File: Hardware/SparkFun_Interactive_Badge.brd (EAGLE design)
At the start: 17.8 x 63.5 mm, 34 parts, among them Q1 DMG2307L, U1 MIC5205-3.3V, U2 ATMEGA328P, U3 CY7C65213

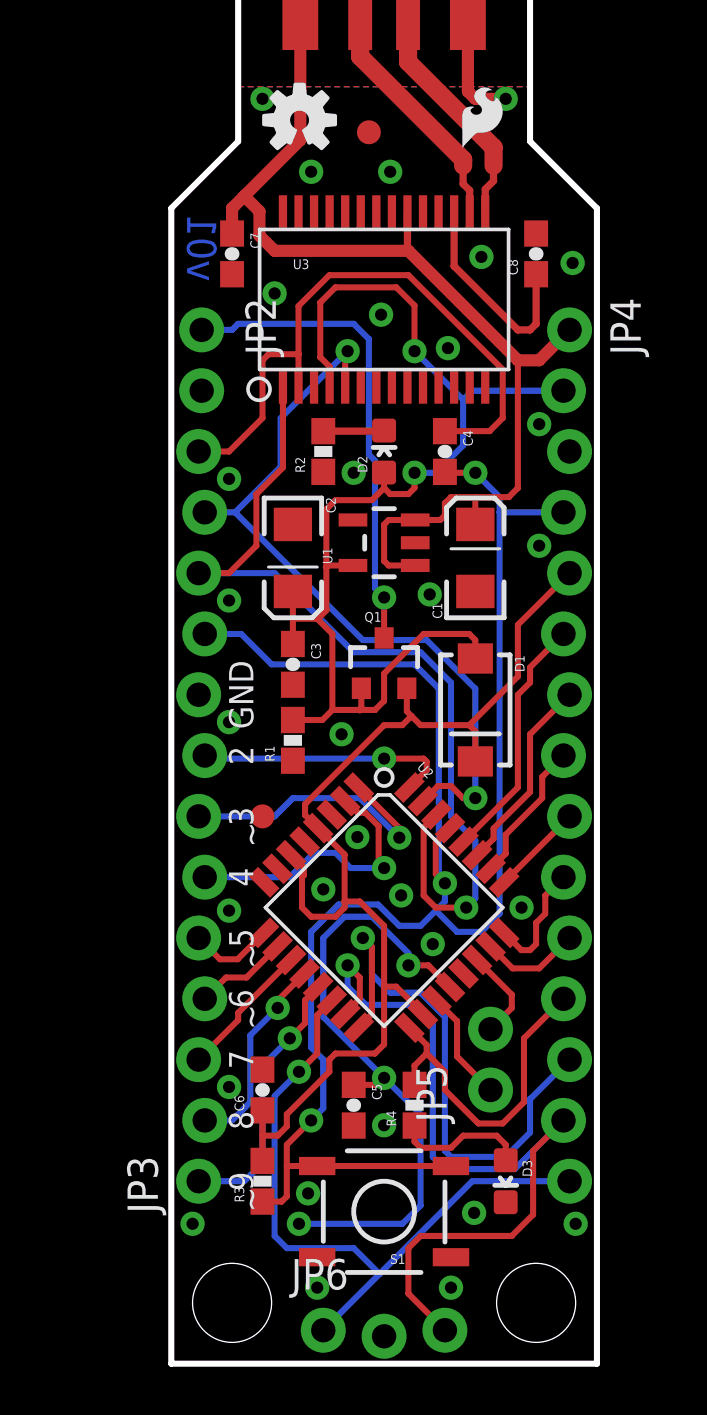
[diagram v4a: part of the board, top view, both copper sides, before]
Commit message: Moved pins. Added silk.
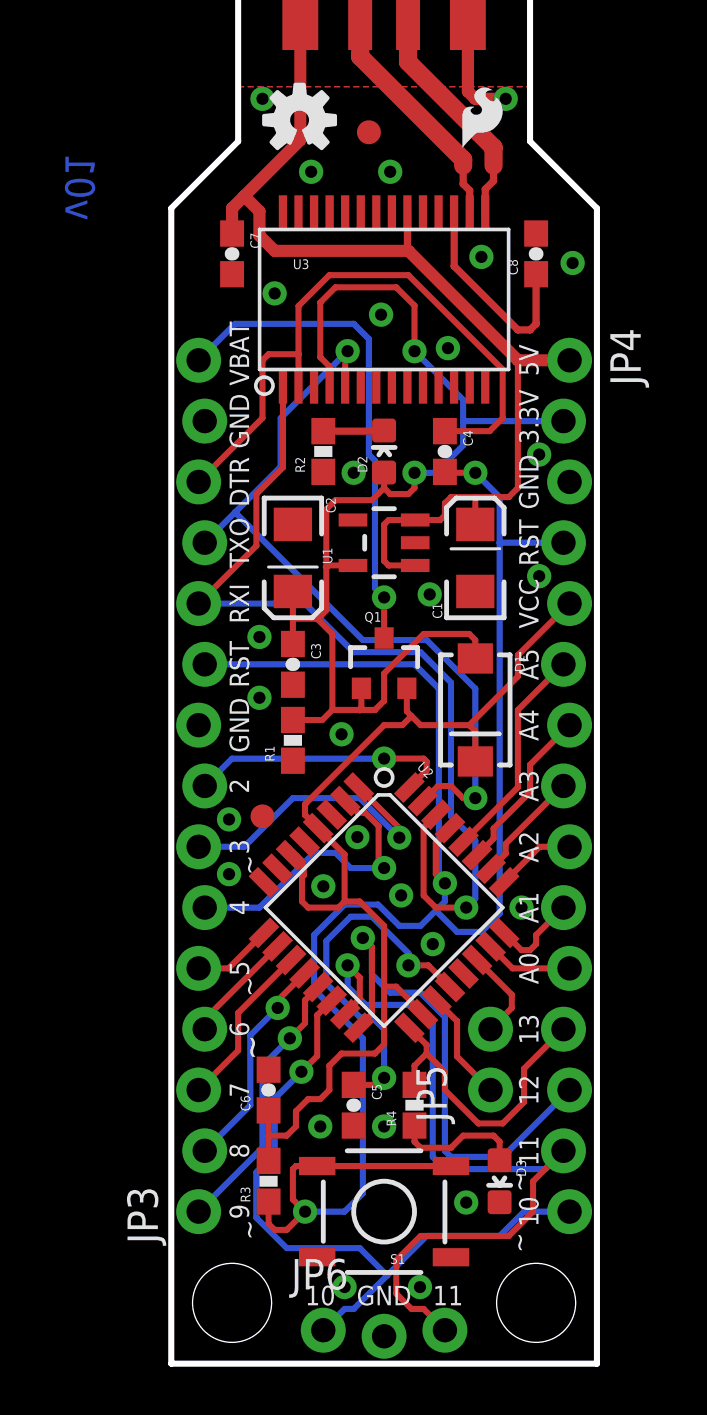
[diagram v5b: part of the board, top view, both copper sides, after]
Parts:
- removed JP2: M021X02_NO_SILK, SparkFun-Connectors:1X02_NO_SILK
- JP3: value M13LOCK_NO_SILK -> M15LOCK_NO_SILK; device SparkFun-Connectors:1X13_LOCK_NO_SILK -> SparkFun-Connectors:1X15_LOCK_NO_SILK
- moved JP4 1.27 mm to (16.5, 41.9)
- moved JP3 1.27 mm to (1.27, 6.35)
- moved D3 0.25 mm to (13.7, 7.62)
- moved C6 0.25 mm to (4.06, 11.4)
- moved R3 0.25 mm to (4.06, 7.62)
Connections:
- net GND: now also JP3.14; no longer JP2.2
- net VBAT: now also JP3.15; no longer JP2.1
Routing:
- net AREF: track 26.8 -> 15.5 mm, vias 3 -> 2
- net RESET: track 75.3 -> 80.7 mm
- net VCC: track 47.5 -> 45.8 mm
- net MISO: track 23.0 -> 21.7 mm
- net A4: track 8.30 -> 7.03 mm
- net A3: track 5.99 -> 4.72 mm
- net SCK: track 14.0 -> 12.7 mm
- net D7: track 5.76 -> 7.03 mm
- net A5: track 10.4 -> 9.14 mm
- net A1: track 5.01 -> 3.74 mm
- net MOSI: track 34.0 -> 32.8 mm
- net D6: track 3.95 -> 4.72 mm
- net VBAT: track 20.1 -> 20.8 mm
- net D8: track 8.54 -> 9.14 mm
- net A2: track 3.89 -> 3.35 mm
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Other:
- board text added: "10"
- board text added: "11"
- board text added: "12"
- board text added: "13"
- board text added: "3.3V"
- board text added: "5V"
- board text added: "A0"
- board text added: "A1"
- board text added: "A2"
- board text added: "A3"
- board text added: "A4"
- board text added: "A5"
- board text added: "Battery"
- board text added: "DTR"
- board text added: "LED Array"
- board text added: "RST"
- board text added: "RXI"
- board text added: "TXO"
- board text added: "VBAT"
- board text added: "VCC"

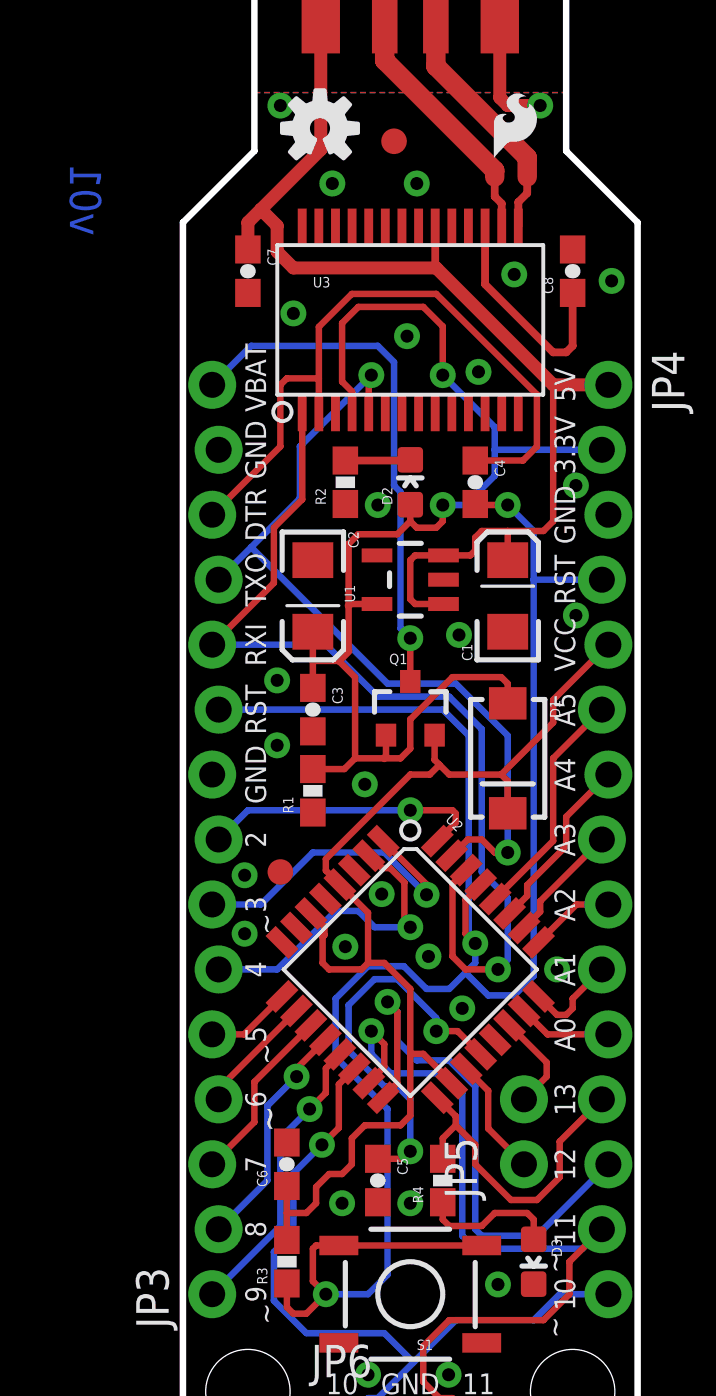
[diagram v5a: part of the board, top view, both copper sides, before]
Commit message: Added bottom silk. Added A6, A7 silk.
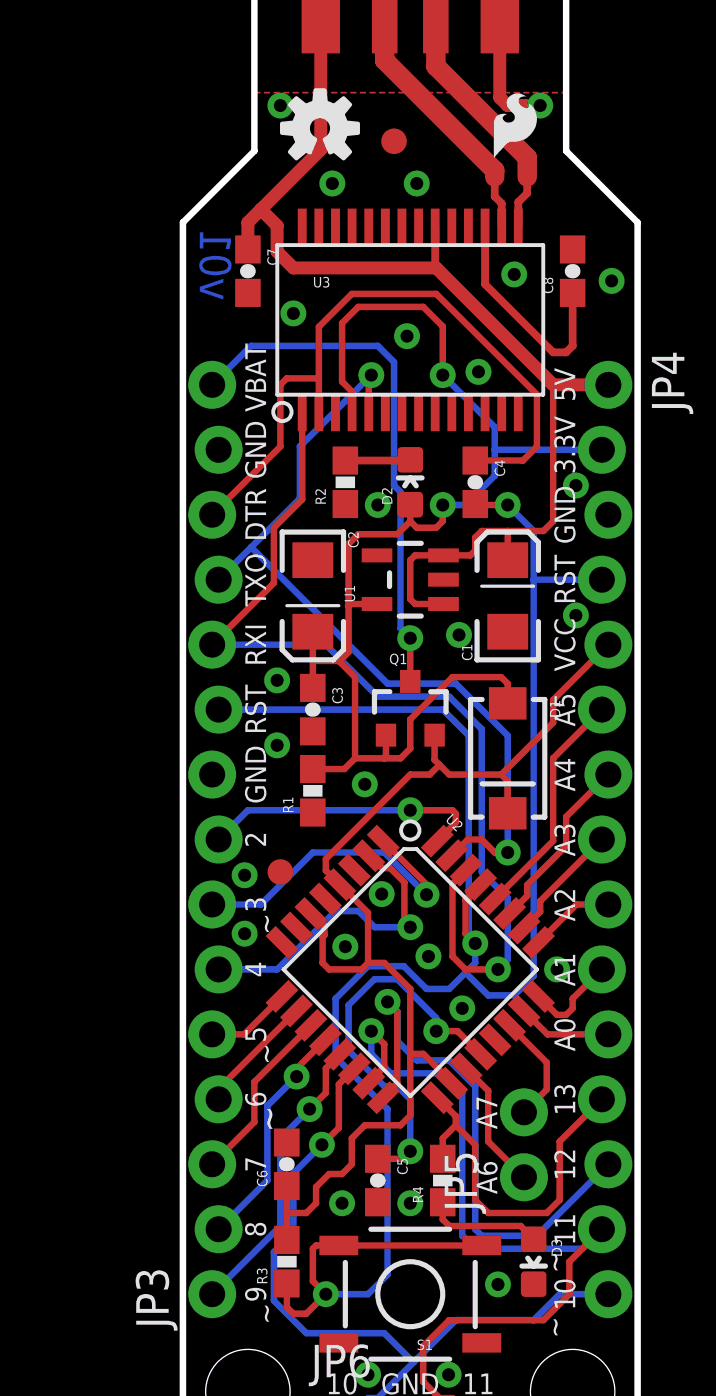
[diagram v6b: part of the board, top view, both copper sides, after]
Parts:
- moved JP5 0.51 mm to (13.3, 10.9)
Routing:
- net SCK: track 12.7 -> 14.5 mm
- net N$1: track 5.42 -> 4.56 mm
- net A7: track 3.86 -> 4.37 mm
- net A6: track 4.67 -> 5.18 mm
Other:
- board text added: "A6"
- board text added: "A7"
- board text added: "Game Port"
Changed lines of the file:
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@@
 <setting verticaltext="up"/>
 </settings>
-<grid distance="0.01" unitdist="inch" unit="inch" style="dots" multiple="1" display="yes" altdistance="0.005" altunitdist="inch" altunit="inch"/>
+<grid distance="0.05" unitdist="inch" unit="inch" style="dots" multiple="1" display="yes" altdistance="0.025" altunitdist="inch" altunit="inch"/>
 <layers>
-<layer number="1" name="Top" color="4" fill="1" visible="no" active="yes"/>
+<layer number="1" name="Top" color="4" fill="1" visible="yes" active="yes"/>
 <layer number="2" name="Route2" color="1" fill="3" visible="no" active="yes"/>
 <layer number="15" name="Route15" color="4" fill="6" visible="no" active="yes"/>
@@
 <layer number="19" name="Unrouted" color="6" fill="1" visible="yes" active="yes"/>
 <layer number="20" name="Dimension" color="15" fill="1" visible="yes" active="yes"/>
-<layer number="21" name="tPlace" color="16" fill="1" visible="no" active="yes"/>
+<layer number="21" name="tPlace" color="16" fill="1" visible="yes" active="yes"/>
 <layer number="22" name="bPlace" color="14" fill="1" visible="yes" active="yes"/>
-<layer number="23" name="tOrigins" color="15" fill="1" visible="no" active="yes"/>
+<layer number="23" name="tOrigins" color="15" fill="1" visible="yes" active="yes"/>
 <layer number="24" name="bOrigins" color="15" fill="1" visible="yes" active="yes"/>
 <layer number="25" name="tNames" color="7" fill="1" visible="no" active="yes"/>
@@
 <layer number="43" name="vRestrict" color="2" fill="10" visible="no" active="yes"/>
 <layer number="44" name="Drills" color="7" fill="1" visible="no" active="yes"/>
-<layer number="45" name="Holes" color="7" fill="1" visible="no" active="yes"/>
+<layer number="45" name="Holes" color="7" fill="1" visible="yes" active="yes"/>
 <layer number="46" name="Milling" color="3" fill="1" visible="no" active="yes"/>
-<layer number="51" name="tDocu" color="6" fill="1" visible="no" active="yes"/>
+<layer number="51" name="tDocu" color="6" fill="1" visible="yes" active="yes"/>
 <layer number="52" name="bDocu" color="7" fill="1" visible="no" active="yes"/>
 <layer number="3" name="Route3" color="4" fill="3" visible="no" active="no"/>
@@
 <text x="2.8194" y="15.748" size="0.8128" layer="21" font="vector" ratio="15" rot="R90" align="top-center">~</text>
 <text x="2.8194" y="20.828" size="0.8128" layer="21" font="vector" ratio="15" rot="R90" align="top-center">~</text>
-<text x="-3.81" y="49.149" size="1.2192" layer="16" font="vector" ratio="15" rot="MR270" align="center">v01</text>
+<text x="1.27" y="46.609" size="1.2192" layer="16" font="vector" ratio="15" rot="MR270" align="center">v01</text>
 <text x="2.4384" y="29.21" size="0.8128" layer="21" font="vector" ratio="15" rot="R90" align="top-center">RST</text>
 <text x="2.4384" y="31.75" size="0.8128" layer="21" font="vector" ratio="15" rot="R90" align="top-center">RXI</text>
@@
 <wire x1="4.572" y1="40.894" x2="4.572" y2="40.386" width="0.254" layer="22"/>
 <text x="6.096" y="40.64" size="1.27" layer="22" font="vector" ratio="15" rot="MR0" align="center-right">Battery</text>
+<text x="8.89" y="4.826" size="1.27" layer="22" font="vector" ratio="15" rot="MR0" align="bottom-center">Game
+Port</text>
+<wire x1="8.89" y1="2.794" x2="8.636" y2="3.048" width="0.254" layer="22"/>
+<wire x1="8.636" y1="3.048" x2="8.382" y2="3.302" width="0.254" layer="22"/>
+<wire x1="8.382" y1="3.302" x2="8.128" y2="3.556" width="0.254" layer="22"/>
+<wire x1="8.128" y1="3.556" x2="8.636" y2="3.556" width="0.254" layer="22"/>
+<wire x1="8.636" y1="3.556" x2="8.89" y2="3.556" width="0.254" layer="22"/>
+<wire x1="8.89" y1="3.556" x2="9.144" y2="3.556" width="0.254" layer="22"/>
+<wire x1="9.144" y1="3.556" x2="9.652" y2="3.556" width="0.254" layer="22"/>
+<wire x1="9.652" y1="3.556" x2="9.398" y2="3.302" width="0.254" layer="22"/>
+<wire x1="9.398" y1="3.302" x2="9.144" y2="3.048" width="0.254" layer="22"/>
+<wire x1="9.144" y1="3.048" x2="8.89" y2="2.794" width="0.254" layer="22"/>
+<wire x1="8.89" y1="3.556" x2="8.89" y2="4.064" width="0.254" layer="22"/>
+<wire x1="9.144" y1="3.556" x2="9.144" y2="4.064" width="0.254" layer="22"/>
+<wire x1="8.636" y1="3.556" x2="8.636" y2="4.064" width="0.254" layer="22"/>
+<wire x1="8.636" y1="4.064" x2="9.144" y2="4.064" width="0.254" layer="22"/>
+<wire x1="8.382" y1="3.302" x2="9.398" y2="3.302" width="0.254" layer="22"/>
+<wire x1="8.636" y1="3.048" x2="9.144" y2="3.048" width="0.254" layer="22"/>
+<text x="12.2936" y="13.462" size="0.8128" layer="21" font="vector" ratio="15" rot="R90" align="bottom-center">A7</text>
+<text x="12.2936" y="10.922" size="0.8128" layer="21" font="vector" ratio="15" rot="R90" align="bottom-center">A6</text>
 </plain>
 <attributes>
@@
 <element name="FRAME1" library="SparkFun-Aesthetics" package="CREATIVE_COMMONS" value="FRAME-LETTER" x="-19.05" y="-10.16"/>
 <element name="JP1" library="SparkFun-Connectors" package="USB-A-PCB" value="USBPCB" x="8.89" y="58.42" rot="R270"/>
-<element name="JP5" library="SparkFun-Connectors" package="1X02_NO_SILK" value="M021X02_NO_SILK" x="13.335" y="11.43" rot="R90"/>
+<element name="JP5" library="SparkFun-Connectors" package="1X02_NO_SILK" value="M021X02_NO_SILK" x="13.335" y="10.922" rot="R90"/>
 <element name="LOGO1" library="SparkFun-Aesthetics" package="SFE_LOGO_FLAME_.1" value="SFE_LOGO_FLAME.1_INCH" x="11.8364" y="50.419"/>
 <element name="LOGO2" library="SparkFun-Aesthetics" package="OSHW-LOGO-S" value="OSHW-LOGOS" x="5.3594" y="51.943"/>
@@
 <contactref element="U2" pad="19"/>
 <contactref element="JP5" pad="1"/>
-<wire x1="13.335" y1="11.43" x2="11.938" y2="12.827" width="0.254" layer="1"/>
-<wire x1="11.938" y1="12.827" x2="11.938" y2="14.304940625" width="0.254" layer="1"/>
+<wire x1="11.938" y1="12.319" x2="11.938" y2="14.304940625" width="0.254" layer="1"/>
 <wire x1="11.938" y1="14.304940625" x2="11.076796875" y2="15.16614375" width="0.254" layer="1"/>
+<wire x1="11.938" y1="12.319" x2="13.335" y2="10.922" width="0.254" layer="1"/>
 </signal>
 <signal name="A7">
 <contactref element="U2" pad="22"/>
 <contactref element="JP5" pad="2"/>
-<wire x1="13.335" y1="13.97" x2="14.224" y2="14.859" width="0.254" layer="1"/>
-<wire x1="14.224" y1="14.859" x2="14.224" y2="15.413053125" width="0.254" layer="1"/>
+<wire x1="14.224" y1="14.351" x2="14.224" y2="15.413053125" width="0.254" layer="1"/>
 <wire x1="14.224" y1="15.413053125" x2="12.773853125" y2="16.8632" width="0.254" layer="1"/>
+<wire x1="14.224" y1="14.351" x2="13.335" y2="13.462" width="0.254" layer="1"/>
 </signal>
 <signal name="RXI">
@@
 <wire x1="10.668" y1="12.954" x2="10.668" y2="13.312196875" width="0.254" layer="1"/>
 <wire x1="10.668" y1="13.312196875" x2="9.945425" y2="14.034771875" width="0.254" layer="1"/>
-<wire x1="14.732" y1="10.922" x2="13.843" y2="10.033" width="0.254" layer="1"/>
-<wire x1="13.843" y1="10.033" x2="12.827" y2="10.033" width="0.254" layer="1"/>
-<wire x1="12.827" y1="10.033" x2="11.43" y2="11.43" width="0.254" layer="1"/>
-<wire x1="11.43" y1="11.43" x2="11.43" y2="12.192" width="0.254" layer="1"/>
 <wire x1="11.43" y1="12.192" x2="10.668" y2="12.954" width="0.254" layer="1"/>
-<wire x1="14.732" y1="10.922" x2="14.732" y2="12.319" width="0.254" layer="1"/>
+<wire x1="14.732" y1="10.033" x2="14.732" y2="12.319" width="0.254" layer="1"/>
 <wire x1="14.732" y1="12.319" x2="16.383" y2="13.97" width="0.254" layer="1"/>
+<wire x1="11.43" y1="12.192" x2="11.43" y2="10.033" width="0.254" layer="1"/>
+<wire x1="11.43" y1="10.033" x2="11.938" y2="9.525" width="0.254" layer="1"/>
+<wire x1="11.938" y1="9.525" x2="14.224" y2="9.525" width="0.254" layer="1"/>
+<wire x1="14.224" y1="9.525" x2="14.732" y2="10.033" width="0.254" layer="1"/>
 </signal>
 <signal name="N$1">
@@
 <wire x1="10.16" y1="9.945" x2="10.16" y2="9.271" width="0.254" layer="1"/>
 <wire x1="10.16" y1="9.271" x2="10.414" y2="9.017" width="0.254" layer="1"/>
-<wire x1="12.192" y1="9.525" x2="11.684" y2="9.017" width="0.254" layer="1"/>
-<wire x1="11.684" y1="9.017" x2="10.414" y2="9.017" width="0.254" layer="1"/>
-<wire x1="13.716" y1="8.497" x2="13.716" y2="9.271" width="0.254" layer="1"/>
-<wire x1="13.716" y1="9.271" x2="13.462" y2="9.525" width="0.254" layer="1"/>
-<wire x1="13.462" y1="9.525" x2="12.192" y2="9.525" width="0.254" layer="1"/>
+<wire x1="13.716" y1="8.497" x2="13.716" y2="8.509" width="0.254" layer="1"/>
+<wire x1="13.716" y1="8.509" x2="13.208" y2="9.017" width="0.254" layer="1"/>
+<wire x1="13.208" y1="9.017" x2="10.414" y2="9.017" width="0.254" layer="1"/>
 </signal>
 <signal name="D+">

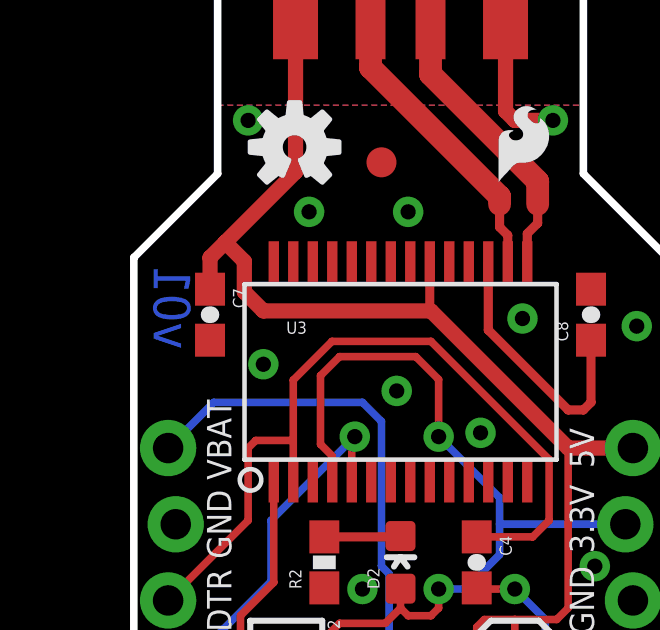
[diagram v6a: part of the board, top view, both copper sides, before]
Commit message: Colored in silk for required headers.
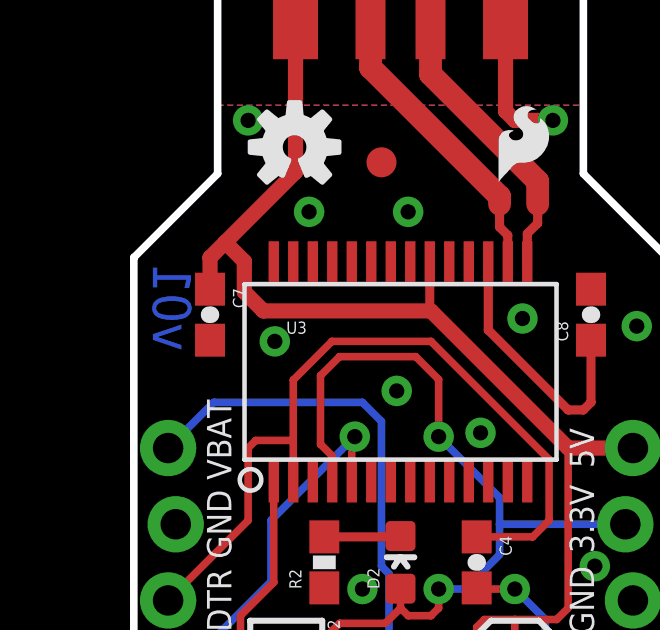
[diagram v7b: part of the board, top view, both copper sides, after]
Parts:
- FRAME1: value FRAME-LETTER -> (none)
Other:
- board text added: "Badger Stick"
- board text removed: "Shawn Hymel"
- board text removed: "v01"
